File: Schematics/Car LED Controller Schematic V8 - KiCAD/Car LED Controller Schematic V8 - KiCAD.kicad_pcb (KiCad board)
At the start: 2 copper layers, 101.9 x 70 mm, 21 parts, among them J1 5V Power In, J2 Select Button, J3 LCD, Relay, LED Signal, J4 ZSS-108-01-F-D-506, J5 DRL, Horn Sense, J6 Reset Button, U1 ESP32-DEVKITC-32D, U2 BOB-12009

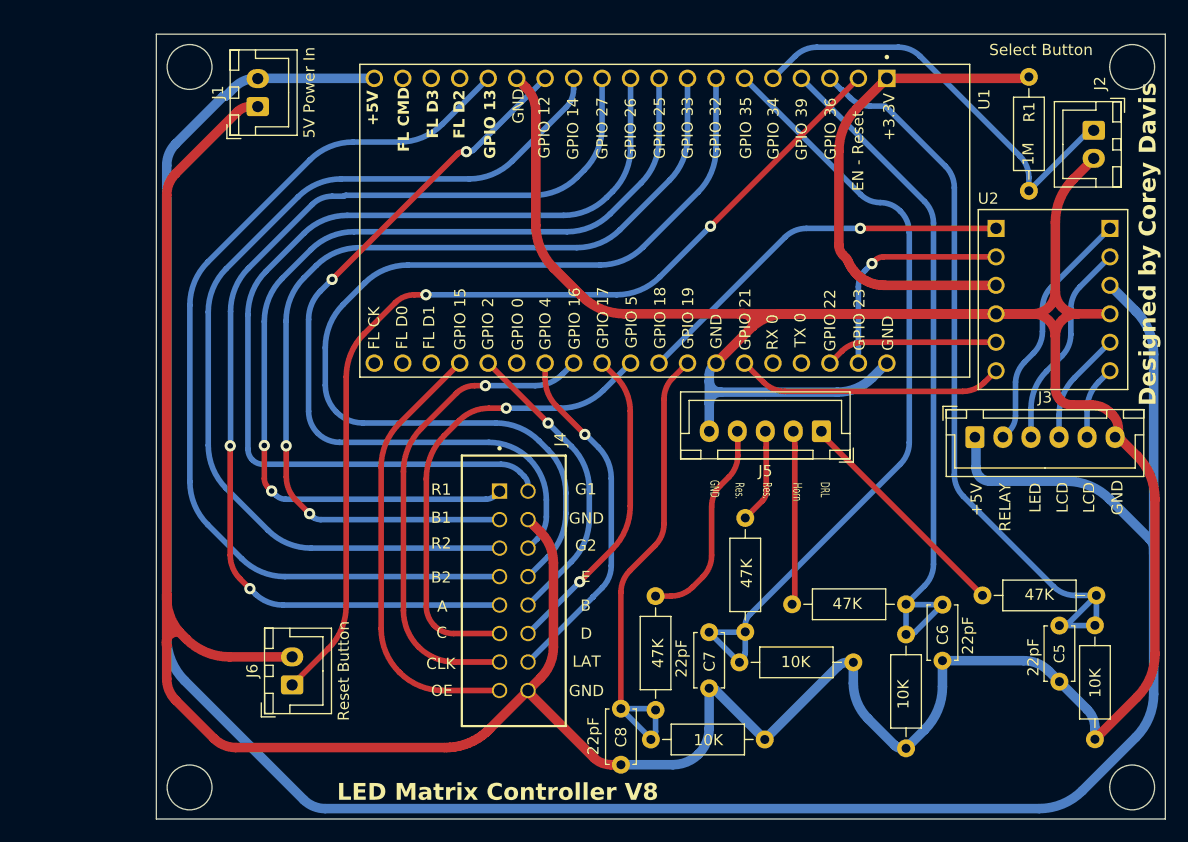
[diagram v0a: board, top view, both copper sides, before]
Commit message: fixed DRC issues
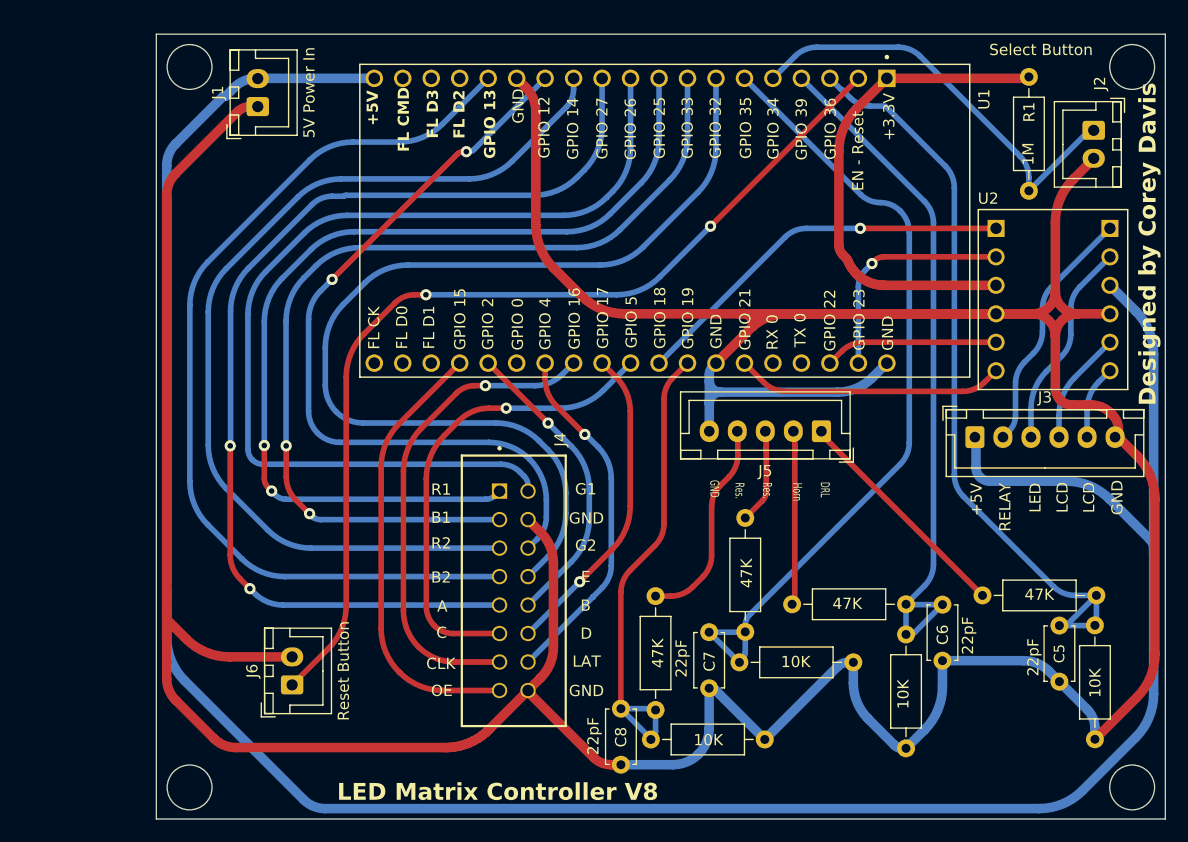
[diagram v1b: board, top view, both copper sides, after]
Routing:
- net GND: track 371.0 -> 368.2 mm

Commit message: whole lotta fun
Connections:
- C7 pad 1: Net-(U1-IO35) -> Net-(U1-IO34)
- C8 pad 1: Net-(U1-IO19) -> Net-(U1-IO35)
- R14 pad 1: Net-(U1-IO35) -> Net-(U1-IO34)
- R15 pad 1: Net-(U1-IO35) -> Net-(U1-IO34)
- R16 pad 1: Net-(U1-IO19) -> Net-(U1-IO35)
- R17 pad 1: Net-(U1-IO19) -> Net-(U1-IO35)
- U1 pad J2-5: Net-(J2-Pin_1) -> Net-(U1-IO34)
- U1 pad J3-8: Net-(U1-IO19) -> Net-(J2-Pin_1)
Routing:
- net Net-(U1-IO34): track 0.00 -> 75.6 mm
- net Net-(U1-IO19): track 42.5 -> 0.00 mm
- net Net-(U1-IO35): track 72.1 -> 85.2 mm
- net Net-(J2-Pin_1): track 38.2 -> 45.7 mm, vias 0 -> 1
- net +3.3V: track 44.9 -> 48.0 mm
- net GND: track 368.2 -> 369.4 mm
- net Net-(J5-Res-Pad4): track 18.5 -> 17.3 mm
- net Net-(U1-SENSOR_VN): track 62.8 -> 63.7 mm
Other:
- board text added: "L.Ind"
- board text added: "R.Ind"
- board text removed: "Res."
